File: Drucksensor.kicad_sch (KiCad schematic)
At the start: 29 parts, among them J101 Conn_01x02, J103 RJ45, J104 RJ45, Q101 Q_NMOS_GSD, Q102 Q_NMOS_GSD, Q103 Q_NMOS_GSD, SW101 SW_SPDT, SW102 SW_SPDT, U101 REF3040

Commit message: Zweiten Wiederstand zu Spannungsteiler hinzugefügt.
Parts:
- added R102, R103, R104: 10k, Resistor_SMD:R_0603_1608Metric, symbol Device:R
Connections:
- net GND: now also R102.2, R103.2, R104.2
- net Magnetron_ADC: now also R103.1
- net Magnetron_Setpoint_ADC: now also R104.1
- net Pirani_ADC: now also R102.1
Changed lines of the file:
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@@
   (junction (at 69.85 129.54) (diameter 1.016) (color 0 0 0 0))
   (junction (at 69.85 142.24) (diameter 1.016) (color 0 0 0 0))
+  (junction (at 69.85 151.13) (diameter 1.016) (color 0 0 0 0))
   (junction (at 71.12 72.39) (diameter 1.016) (color 0 0 0 0))
   (junction (at 106.68 139.7) (diameter 1.016) (color 0 0 0 0))
@@
     (stroke (width 0) (type solid) (color 0 0 0 0))
   )
+  (wire (pts (xy 69.85 90.17) (xy 69.85 96.52))
+    (stroke (width 0) (type solid) (color 0 0 0 0))
+  )
   (wire (pts (xy 69.85 90.17) (xy 71.12 90.17))
     (stroke (width 0) (type solid) (color 0 0 0 0))
   )
+  (wire (pts (xy 69.85 96.52) (xy 71.12 96.52))
+    (stroke (width 0) (type solid) (color 0 0 0 0))
+  )
   (wire (pts (xy 69.85 121.92) (xy 69.85 129.54))
     (stroke (width 0) (type solid) (color 0 0 0 0))
   )
+  (wire (pts (xy 69.85 129.54) (xy 69.85 133.35))
+    (stroke (width 0) (type solid) (color 0 0 0 0))
+  )
   (wire (pts (xy 69.85 129.54) (xy 71.12 129.54))
     (stroke (width 0) (type solid) (color 0 0 0 0))
   )
+  (wire (pts (xy 69.85 133.35) (xy 71.12 133.35))
+    (stroke (width 0) (type solid) (color 0 0 0 0))
+  )
   (wire (pts (xy 69.85 142.24) (xy 69.85 151.13))
     (stroke (width 0) (type solid) (color 0 0 0 0))
   )
   (wire (pts (xy 69.85 142.24) (xy 71.12 142.24))
+    (stroke (width 0) (type solid) (color 0 0 0 0))
+  )
+  (wire (pts (xy 69.85 151.13) (xy 69.85 157.48))
+    (stroke (width 0) (type solid) (color 0 0 0 0))
+  )
+  (wire (pts (xy 69.85 157.48) (xy 71.12 157.48))
     (stroke (width 0) (type solid) (color 0 0 0 0))
   )
@@
     (pin "1")
   )
+  (symbol (lib_id "power:GND") (at 78.74 96.52 90) (unit 1)
+    (in_bom yes) (on_board yes) (fields_autoplaced)
+    (property "Reference" "#PWR0107" (id 0) (at 85.09 96.52 0)
+      (effects (font (size 1.27 1.27)) hide)
+    )
+    (property "Value" "GND" (id 1) (at 81.9151 96.9085 90)
+      (effects (font (size 1.27 1.27)) (justify right))
+    )
+    (property "Footprint" "" (id 2) (at 78.74 96.52 0)
+      (effects (font (size 1.27 1.27)) hide)
+    )
+    (property "Datasheet" "" (id 3) (at 78.74 96.52 0)
+      (effects (font (size 1.27 1.27)) hide)
+    )
+    (pin "1")
+  )
   (symbol (lib_id "power:GND") (at 78.74 121.92 90) (unit 1)
     (in_bom yes) (on_board yes)
@@
     (pin "1")
   )
+  (symbol (lib_id "power:GND") (at 78.74 133.35 90) (unit 1)
+    (in_bom yes) (on_board yes) (fields_autoplaced)
+    (property "Reference" "#PWR0108" (id 0) (at 85.09 133.35 0)
+      (effects (font (size 1.27 1.27)) hide)
+    )
+    (property "Value" "GND" (id 1) (at 81.9151 133.7385 90)
+      (effects (font (size 1.27 1.27)) (justify right))
+    )
+    (property "Footprint" "" (id 2) (at 78.74 133.35 0)
+      (effects (font (size 1.27 1.27)) hide)
+    )
+    (property "Datasheet" "" (id 3) (at 78.74 133.35 0)
+      (effects (font (size 1.27 1.27)) hide)
+    )
+    (pin "1")
+  )
   (symbol (lib_id "power:GND") (at 78.74 142.24 90) (unit 1)
     (in_bom yes) (on_board yes) (fields_autoplaced)
@@
     )
     (property "Datasheet" "" (id 3) (at 78.74 151.13 0)
+      (effects (font (size 1.27 1.27)) hide)
+    )
+    (pin "1")
+  )
+  (symbol (lib_id "power:GND") (at 78.74 157.48 90) (unit 1)
+    (in_bom yes) (on_board yes) (fields_autoplaced)
+    (property "Reference" "#PWR0109" (id 0) (at 85.09 157.48 0)
+      (effects (font (size 1.27 1.27)) hide)
+    )
+    (property "Value" "GND" (id 1) (at 81.9151 157.8685 90)
+      (effects (font (size 1.27 1.27)) (justify right))
+    )
+    (property "Footprint" "" (id 2) (at 78.74 157.48 0)
+      (effects (font (size 1.27 1.27)) hide)
+    )
+    (property "Datasheet" "" (id 3) (at 78.74 157.48 0)
       (effects (font (size 1.27 1.27)) hide)
     )
@@
     (pin "2")
   )
+  (symbol (lib_id "Device:R") (at 74.93 96.52 90) (unit 1)
+    (in_bom yes) (on_board yes) (fields_autoplaced)
+    (property "Reference" "R102" (id 0) (at 74.93 92.0708 90))
+    (property "Value" "10k" (id 1) (at 74.93 94.3695 90))
+    (property "Footprint" "Resistor_SMD:R_0603_1608Metric" (id 2) (at 74.93 98.298 90)
+      (effects (font (size 1.27 1.27)) hide)
+    )
+    (property "Datasheet" "~" (id 3) (at 74.93 96.52 0)
+      (effects (font (size 1.27 1.27)) hide)
+    )
+    (pin "1")
+    (pin "2")
+  )
   (symbol (lib_id "Device:R") (at 74.93 129.54 90) (unit 1)
     (in_bom yes) (on_board yes) (fields_autoplaced)
@@
     (pin "2")
   )
+  (symbol (lib_id "Device:R") (at 74.93 133.35 90) (unit 1)
+    (in_bom yes) (on_board yes) (fields_autoplaced)
+    (property "Reference" "R103" (id 0) (at 74.93 128.9008 90))
+    (property "Value" "10k" (id 1) (at 74.93 131.1995 90))
+    (property "Footprint" "Resistor_SMD:R_0603_1608Metric" (id 2) (at 74.93 135.128 90)
+      (effects (font (size 1.27 1.27)) hide)
+    )
+    (property "Datasheet" "~" (id 3) (at 74.93 133.35 0)
+      (effects (font (size 1.27 1.27)) hide)
+    )
+    (pin "1")
+    (pin "2")
+  )
   (symbol (lib_id "Device:R") (at 74.93 142.24 90) (unit 1)
     (in_bom yes) (on_board yes) (fields_autoplaced)
@@
     )
     (property "Datasheet" "~" (id 3) (at 74.93 142.24 0)
+      (effects (font (size 1.27 1.27)) hide)
+    )
+    (pin "1")
+    (pin "2")
+  )
+  (symbol (lib_id "Device:R") (at 74.93 157.48 90) (unit 1)
+    (in_bom yes) (on_board yes) (fields_autoplaced)
+    (property "Reference" "R104" (id 0) (at 74.93 153.0308 90))
+    (property "Value" "10k" (id 1) (at 74.93 155.3295 90))
+    (property "Footprint" "Resistor_SMD:R_0603_1608Metric" (id 2) (at 74.93 159.258 90)
+      (effects (font (size 1.27 1.27)) hide)
+    )
+    (property "Datasheet" "~" (id 3) (at 74.93 157.48 0)
       (effects (font (size 1.27 1.27)) hide)
     )
@@
       (reference "#PWR0106") (unit 1) (value "+5V") (footprint "")
     )
+    (path "/bbef8239-242a-4b2c-90a8-0e5355e022eb"
+      (reference "#PWR0107") (unit 1) (value "GND") (footprint "")
+    )
+    (path "/15d095d9-c518-4044-8373-2072b6e0bd3d"
+      (reference "#PWR0108") (unit 1) (value "GND") (footprint "")
+    )
+    (path "/e064a971-4494-4d91-8785-b4ec8979572f"
+      (reference "#PWR0109") (unit 1) (value "GND") (footprint "")
+    )
     (path "/2d02ab7d-f926-4ea3-a20b-4f2275069ede"
       (reference "#PWR0114") (unit 1) (value "GND") (footprint "")
@@
       (reference "R101") (unit 1) (value "470") (footprint "Resistor_SMD:R_0603_1608Metric")
     )
+    (path "/46d79db3-8f8c-4aca-a68d-0ba4259d2b25"
+      (reference "R102") (unit 1) (value "10k") (footprint "Resistor_SMD:R_0603_1608Metric")
+    )
+    (path "/0fafd9ed-b4e5-4a31-9141-b309f564e47f"
+      (reference "R103") (unit 1) (value "10k") (footprint "Resistor_SMD:R_0603_1608Metric")
+    )
+    (path "/015fecbc-b937-4354-b975-a92eb0e1747e"
+      (reference "R104") (unit 1) (value "10k") (footprint "Resistor_SMD:R_0603_1608Metric")
+    )
     (path "/5718552a-9e5a-425c-a6b2-49137faa0f65"

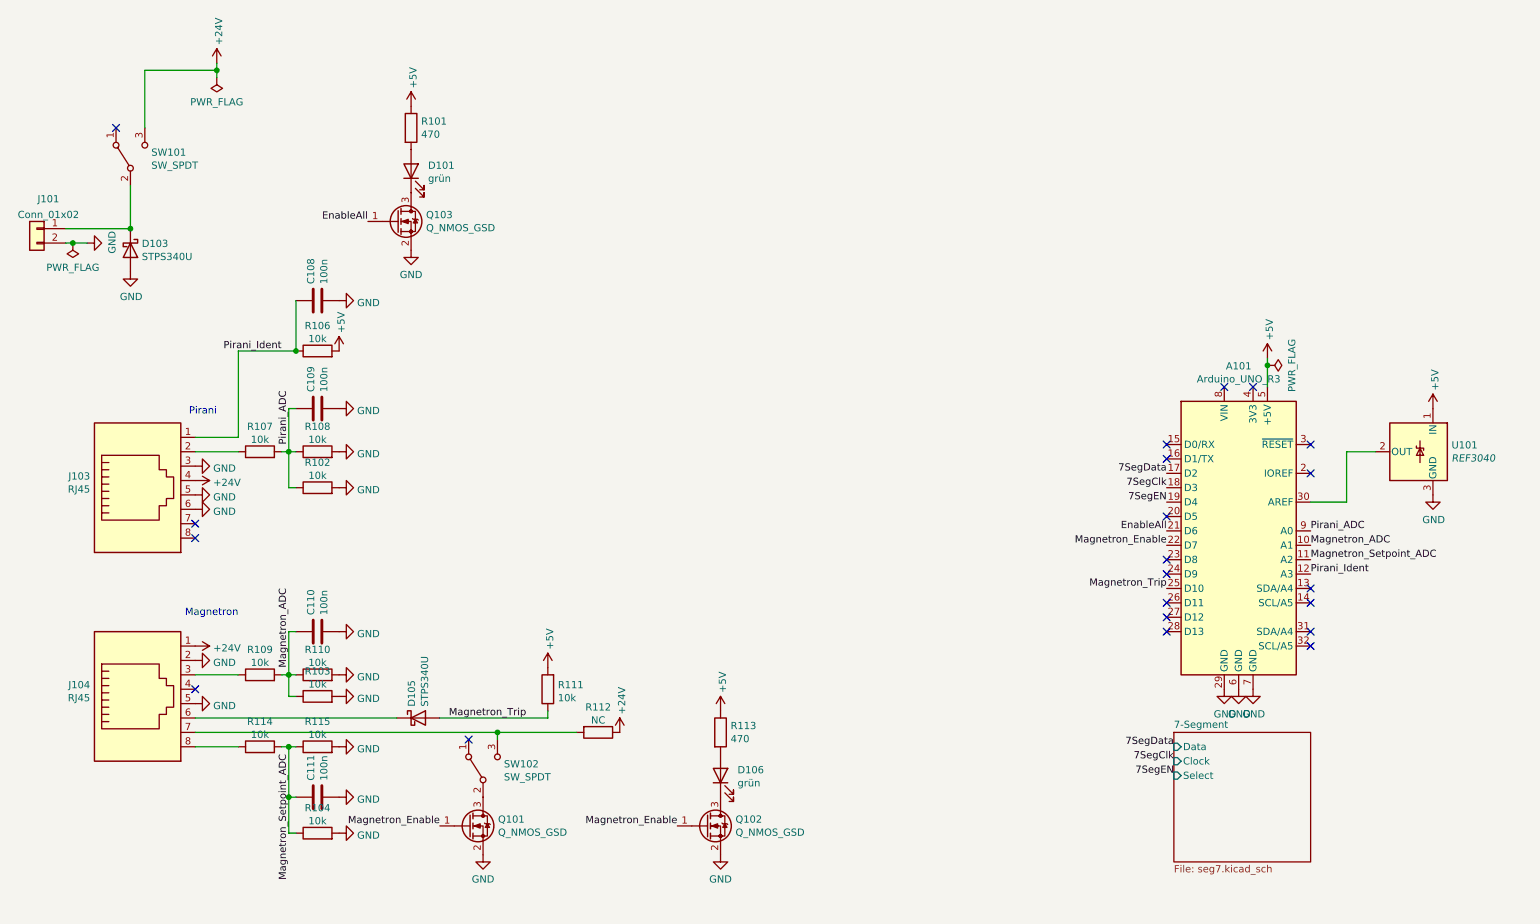
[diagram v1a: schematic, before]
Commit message: RS232 hinzugefügt
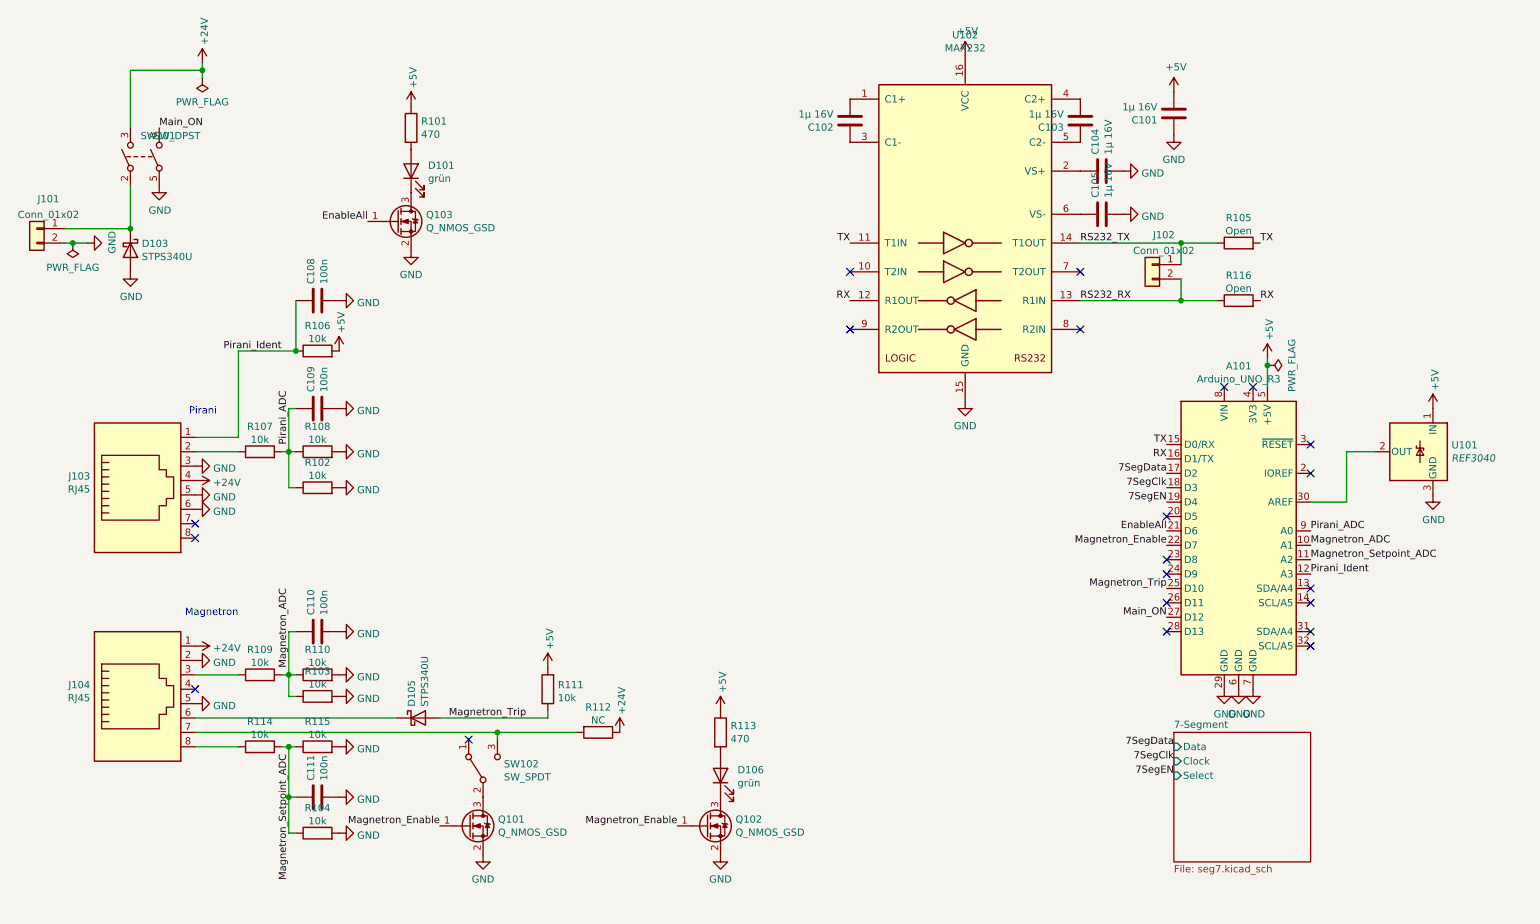
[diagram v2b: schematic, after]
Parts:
- removed SW101: SW_SPDT, Sven:Switch_DPDT, symbol Switch:SW_SPDT
- added C101, C102, C103, C104, C105: 1µ 16V, Capacitor_SMD:C_0805_2012Metric, symbol Device:C
- added J102: Conn_01x02, TerminalBlock:TerminalBlock_bornier-2_P5.08mm, symbol Connector_Generic:Conn_01x02
- added R105, R116: Open, Resistor_SMD:R_0805_2012Metric, symbol Device:R
- added SW101: SW_DPST, Sven:Switch_DPDT, symbol Switch:SW_DPST
- added U102: MAX232, Package_SO:SOIC-16W_7.5x10.3mm_P1.27mm, symbol Interface_UART:MAX232
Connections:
- net +24V: now also SW101.3
- net +5V: now also C101.2, U102.16 (VCC)
- net GND: now also C101.1, C104.2, C105.2, SW101.5, U102.15 (GND)
- net at D103.1 (K), J101.1 (Pin_1): now also SW101.2
- net TX: now reaches A101.15 (D0/RX)
- net TX: now also R105.2, U102.11 (T1IN)
- net RX: now reaches A101.16 (D1/TX)
- net RX: now also R116.2, U102.12 (R1OUT)
- net Main_ON: now reaches A101.27 (D12)
- net Main_ON: now also SW101.6
- new net: C102.2, U102.1 (C1+)
- new net: C104.1, U102.2 (VS+)
- new net: C102.1, U102.3 (C1-)
- new net: C103.2, U102.4 (C2+)
- new net: C103.1, U102.5 (C2-)
- new net: C105.1, U102.6 (VS-)
- new net RS232_RX: J102.2 (Pin_2), R116.1, U102.13 (R1IN)
- new net RS232_TX: J102.1 (Pin_1), R105.1, U102.14 (T1OUT)

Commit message: Anschluss für Edwards-Turbopumpe hinzugefügt
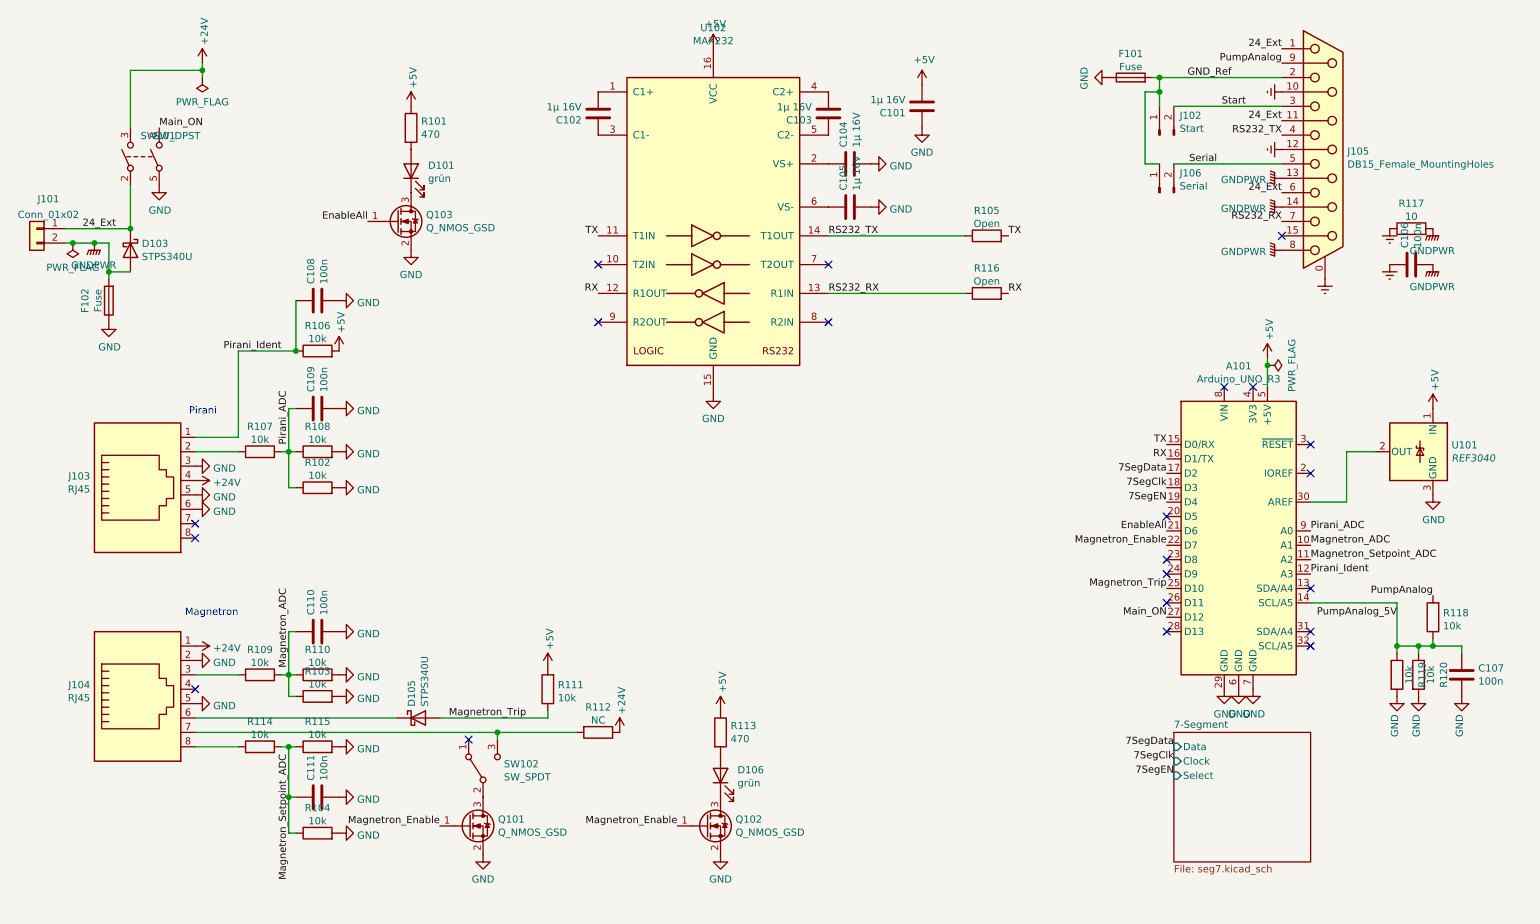
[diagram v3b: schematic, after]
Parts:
- removed J102: Conn_01x02, TerminalBlock:TerminalBlock_bornier-2_P5.08mm, symbol Connector_Generic:Conn_01x02
- added C106, C107: 100n, Capacitor_SMD:C_0603_1608Metric, symbol Device:C
- added F101, F102: Fuse, Resistor_SMD:R_1210_3225Metric, symbol Device:Fuse
- added J102: Start, Connector_PinSocket_2.54mm:PinSocket_1x02_P2.54mm_Vertical, symbol Connector:Conn_01x02_Male
- added J105: DB15_Female_MountingHoles, Connector_Dsub:DSUB-15_Female_Vertical_P2.77x2.84mm_MountingHoles, symbol Connector:DB15_Female_MountingHoles
- added J106: Serial, Connector_PinSocket_2.54mm:PinSocket_1x02_P2.54mm_Vertical, symbol Connector:Conn_01x02_Male
- added R117: 10, Resistor_SMD:R_0603_1608Metric, symbol Device:R
- added R118, R119, R120: 10k, Resistor_SMD:R_0603_1608Metric, symbol Device:R
- J101: footprint TerminalBlock:TerminalBlock_bornier-2_P5.08mm -> TerminalBlock:TerminalBlock_bornier-4_P5.08mm
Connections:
- net GND: now also C107.2, F101.1, F102.1, R119.2, R120.2; no longer D103.2 (A), J101.2 (Pin_2)
- net RS232_RX: now also J105.7
- net RS232_TX: now also J105.4
- net 24_Ext: now reaches D103.1 (K), J101.1 (Pin_1), SW101.2
- net 24_Ext: now also J105.1, J105.11 (P111), J105.6
- net PumpAnalog_5V: now reaches A101.14 (SCL/A5)
- net PumpAnalog_5V: now also C107.1, R118.1, R119.1, R120.1
- new net Earth: C106.1, J105.0 (PAD), J105.10 (P10), J105.12 (P12), R117.1
- new net GNDPWR: C106.2, D103.2 (A), F102.2, J101.2 (Pin_2), J105.13 (P13), J105.14 (P14), J105.8, R117.2
- new net GND_Ref: F101.2, J102.1 (Pin_1), J105.2, J106.1 (Pin_1)
- new net PumpAnalog: J105.9 (P9), R118.2
- new net Serial: J105.5, J106.2 (Pin_2)
- new net Start: J102.2 (Pin_2), J105.3
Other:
- moved on the sheet: C101, C102, C103, C104, C105, R105, R116, U102
